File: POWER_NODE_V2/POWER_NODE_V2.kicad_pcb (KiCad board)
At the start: 2 copper layers, 178 x 144 mm, 125 parts, among them J1 CONN_01X02, J10 CONN_02X07, J11 CONN_01X04, J12 CONN_01X04, J13 CONN_01X02, J14 CONN_01X02, J15 CONN_01X02, J16 CONN_01X03, J17 CONN_01X03, J18 CONN_01X03, J19 CONN_01X03, J2 CONN_01X02, J20 CONN_01X03, J21 CONN_01X03, J3 CONN_01X02, J4 CONN_01X02, J5 Booster_J1_J3, J6 I2C2_J10_8_9, J7 Booster_J4_J2, J8 CONN_01X01, J9 CONN_01X02, Q1 BSS84, Q2 BSS84, Q3 BSS84, Q4 BSS84, Q5 BSS84, Q6 BSS84, Q7 BSS84, U1 LM1117MP-3.3/NOPB, U10 DS2482S-100+T&R, U11 DS2482S-100+T&R, U12 NCV8405ADTRKG, U13 MAX14850AEE+, U14 MAX14850AEE+, U15 TL783CKTTR, U16 TL783CKTTR, U17 AMC1100DWV, U18 AMC1100DWV, U19 NUD3124LT1G, U2 R-745.0P, U20 RTE24024, U3 DS2482S-100+T&R, U4 DS2482S-100+T&R, U5 DS2482S-100+T&R, U6 TSYS01, U7 MS5607-02BA03, U8 DS2482S-100+T&R, U9 DS2482S-100+T&R

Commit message: Power Node v2 WIP
TODO: 3d models, double check everything, update connector P/N on
schematics, align boards and drill holes
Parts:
- J1, J13, J14, J15, J2, J9: footprint Pin_Headers:Pin_Header_Straight_1x02_Pitch2.54mm -> rLoop Footprints:TE_1744055-2_3.96_EP_HDR_ASSY_2P_VERT_HT
- J11, J12: footprint Pin_Headers:Pin_Header_Straight_1x04_Pitch2.54mm -> rLoop Footprints:22-04-1041_Molex_4_Pin_Header_2.50mm
- J16, J17, J18, J19, J20, J21: footprint Pin_Headers:Pin_Header_Straight_1x03_Pitch2.54mm -> rLoop Footprints:3-641215-3_3Pin_Latching_Header
- J3, J4: footprint Pin_Headers:Pin_Header_Straight_1x02_Pitch2.54mm -> rLoop Footprints:Keystone_3544-2
- J5: footprint Pin_Headers:Pin_Header_Straight_2x10_Pitch2.54mm -> rLoop Footprints:Booster1_Header_J1_J3
- J6: footprint Pin_Headers:Pin_Header_Straight_1x02_Pitch2.54mm -> Pin_Headers:Pin_Header_Straight_1x02_Pitch2.54mm_SMD_Pin1Left
- J7: footprint Pin_Headers:Pin_Header_Straight_2x10_Pitch2.54mm -> rLoop Footprints:Booster1_J4_J2
- U1: footprint TO_SOT_Packages_SMD:SOT-223-3Lead_TabPin2 -> TO_SOT_Packages_SMD:SOT-223
- U15, U16: footprint TO_SOT_Packages_SMD:TO-263-3_TabPin2 -> TO_SOT_Packages_SMD:TO-263-3_TabPin4
- U2: footprint Socket_Strips:Socket_Strip_Straight_1x12_Pitch2.54mm -> rLoop Footprints:R-745.0P
- moved R13 181.5 mm to (111.2, 35.0)
- moved C21 166.6 mm to (130.0, 147.2), turned to 180 degrees
- moved C23 151.0 mm to (110.2, 157.8)
- moved C24 149.2 mm to (106.5, 157.8)
- moved C22 147.1 mm to (132.5, 138.8), turned to 90 degrees
- moved C27 146.8 mm to (97.8, 57.8), turned to 270 degrees
- moved D6 146.7 mm to (58.2, 29.0), turned to 0 degrees
- moved C26 143.2 mm to (117.8, 157.8)
- moved C20 141.0 mm to (96.0, 157.2), turned to 180 degrees
- moved C25 140.9 mm to (114.0, 157.8)
- moved J13 140.9 mm to (120.5, 29.0), turned to 180 degrees
- moved R20 140.0 mm to (109.5, 155.5), turned to 90 degrees
- moved C14 138.7 mm to (88.0, 150.5)
- moved J9 136.9 mm to (99.0, 29.0), turned to 180 degrees
- moved C19 135.7 mm to (96.2, 147.2), turned to 180 degrees
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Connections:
- C21 pad 1: Net-(C21-Pad1) -> +3V3
- C21 pad 2: Net-(C21-Pad2) -> GND
- C22 pad 1: Net-(C22-Pad1) -> +3V3
- C22 pad 2: Net-(C22-Pad2) -> GND
- C23 pad 1: /Charger Interface/CHG_I_REF -> Net-(C23-Pad1)
- C24 pad 1: /Charger Interface/CHG_I -> Net-(C24-Pad1)
- C25 pad 1: /Charger Interface/BATT_I_REF -> Net-(C25-Pad1)
- C26 pad 1: /Charger Interface/BATT_I -> Net-(C26-Pad1)
- J11 pad 1: Net-(J11-Pad1) -> Net-(C23-Pad1)
- J11 pad 2: Net-(J11-Pad2) -> Net-(C24-Pad1)
- J12 pad 1: Net-(J12-Pad1) -> Net-(C25-Pad1)
- J12 pad 2: Net-(J12-Pad2) -> Net-(C26-Pad1)
- J7 pad 11: /BMS Interface/BMS_ALERT -> /DC Watchdog/DC_WATCHDOG
- J7 pad 17: /DC Watchdog/DC_WATCHDOG -> Net-(J7-Pad17)
- J7 pad 19: Net-(J7-Pad19) -> /BMS Interface/BMS_ALERT
- Q6 pad 3: Net-(Q6-Pad3) -> +3V3
- R17 pad 1: Net-(J11-Pad2) -> Net-(C24-Pad1)
- R18 pad 1: Net-(J12-Pad1) -> Net-(C25-Pad1)
- R19 pad 1: Net-(J12-Pad2) -> Net-(C26-Pad1)
- R20 pad 1: Net-(J11-Pad1) -> Net-(C23-Pad1)
- R21 pad 1: Net-(J11-Pad1) -> /Charger Interface/CHG_I_REF
- R22 pad 1: Net-(J11-Pad2) -> /Charger Interface/CHG_I
- R23 pad 1: Net-(J12-Pad1) -> /Charger Interface/BATT_I_REF
- R24 pad 1: Net-(J12-Pad2) -> /Charger Interface/BATT_I
- R8 pad 2: Net-(R8-Pad2) -> /I2C Devices/I2C2_SCL
- R9 pad 2: Net-(R9-Pad2) -> /I2C Devices/I2C2_SDA
- U10 pad 1: Net-(U10-Pad1) -> +3V3
- U10 pad 4: Net-(R8-Pad2) -> /I2C Devices/I2C2_SCL
- U10 pad 5: Net-(R9-Pad2) -> /I2C Devices/I2C2_SDA
- U11 pad 4: Net-(R8-Pad2) -> /I2C Devices/I2C2_SCL
- U11 pad 5: Net-(R9-Pad2) -> /I2C Devices/I2C2_SDA
- U18 pad 2: Net-(R15-Pad1) -> CHARGE_N_HOT
- U3 pad 4: /I2C Devices/I2C1_SCL -> /I2C Devices/I2C1_SDA
- U3 pad 5: /I2C Devices/I2C1_SDA -> /I2C Devices/I2C1_SCL
- U4 pad 1: Net-(U4-Pad1) -> +3V3
- U7 pad 7: /I2C Devices/I2C1_SDA -> /I2C Devices/I2C1_SCL
- U7 pad 8: /I2C Devices/I2C1_SCL -> /I2C Devices/I2C1_SDA
- U8 pad 4: Net-(R8-Pad2) -> /I2C Devices/I2C2_SCL
- U8 pad 5: Net-(R9-Pad2) -> /I2C Devices/I2C2_SDA
- U9 pad 4: Net-(R8-Pad2) -> /I2C Devices/I2C2_SCL
- U9 pad 5: Net-(R9-Pad2) -> /I2C Devices/I2C2_SDA
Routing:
- net +3V3: track 0.00 -> 509.9 mm, vias 0 -> 13
- net +24V: track 0.00 -> 199.7 mm
- net +5V: track 0.00 -> 130.8 mm
- net Net-(C26-Pad1): track 0.00 -> 117.0 mm
- net /RM57 Core/CHG_RLY: track 0.00 -> 112.9 mm
- net Net-(C23-Pad1): track 0.00 -> 112.2 mm
- net Net-(C24-Pad1): track 0.00 -> 111.9 mm
- net Net-(C25-Pad1): track 0.00 -> 111.6 mm
- net /1-Wire Connectors/ONE_WIRE_BATT_10_12: track 0.00 -> 110.4 mm
- net /BMS Interface/BMS_MISO: track 0.00 -> 108.9 mm, vias 0 -> 2
- net /BMS Interface/BMS_MOSI: track 0.00 -> 107.9 mm, vias 0 -> 2
- net /1-Wire Connectors/ONE_WIRE_BATT_7_9: track 0.00 -> 104.1 mm
- net /BMS Interface/BMS_NCS: track 0.00 -> 100.0 mm, vias 0 -> 2
- net /BMS Interface/BMS_DRDY: track 0.00 -> 94.4 mm, vias 0 -> 2
- net /1-Wire Connectors/ONE_WIRE_BATT_13_15: track 0.00 -> 93.5 mm
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- added copper zone on F.Cu, net +24V
- added copper zone on B.Cu, net GND
- added copper zone on F.Cu, net GND
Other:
- net class 24V_High_Current added: clearance 0.2, trace_width 10, via_dia 12, via_drill 10
- net class Default: via_dia 0.6 -> 0.6858; via_drill 0.4 -> 0.3302
- rule trace_min: 0.2 -> 0.1524
- rule via_min_drill: 0.3 -> 0.3302
- rule via_min_size: 0.4 -> 0.6858

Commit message: 3d WIP
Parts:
- U20: footprint rLoop Footprints:RTE24024 -> rLoop_Footprints:RTE24024
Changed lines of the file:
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@@
   )
   (setup
-    (last_trace_width 2)
+    (last_trace_width 0.25)
     (user_trace_width 2)
     (user_trace_width 4)
@@
     )
   )
-  (module "rLoop Footprints:RTE24024" (layer F.Cu)
-    (at 45.25 80.75 90)
-    (fp_text reference U20 (at 0 8.8 90) (layer F.SilkS)
-      (effects (font (size 1 1) (thickness 0.15)))
-    )
-    (fp_text value RTE24024 (at 0 -8.8 90) (layer F.Fab)
-      (effects (font (size 1 1) (thickness 0.15)))
-    )
-    (fp_line (start -7.56 -7.5) (end 22.68 -7.5) (layer F.SilkS) (width 0.1))
-    (fp_line (start 22.68 -7.5) (end 22.68 7.5) (layer F.SilkS) (width 0.1))
-    (fp_line (start 22.68 7.5) (end -7.56 7.5) (layer F.SilkS) (width 0.1))
-    (fp_line (start -7.56 7.5) (end -7.56 -7.5) (layer F.SilkS) (width 0.1))
-    (pad A2 thru_hole circle (at -5.18 3.75 90) (size 2 2) (drill 1.3) (layers *.Cu *.Mask)
-      (net 19 "Net-(D7-Pad2)"))
-    (pad A1 thru_hole circle (at -5.18 -3.75 90) (size 2 2) (drill 1.3) (layers *.Cu *.Mask)
-      (net 3 +24V))
-    (pad 11 thru_hole circle (at 15.12 -3.75 90) (size 2 2) (drill 1.3) (layers *.Cu *.Mask)
-      (net 3 +24V))
-    (pad 14 thru_hole circle (at 20.16 -3.75 90) (size 2 2) (drill 1.3) (layers *.Cu *.Mask)
-      (net 20 "Net-(D8-Pad2)"))
-    (pad 24 thru_hole circle (at 20.16 3.75 90) (size 2 2) (drill 1.3) (layers *.Cu *.Mask)
-      (net 103 "Net-(U20-Pad24)"))
-    (pad 21 thru_hole circle (at 15.12 3.75 90) (size 2 2) (drill 1.3) (layers *.Cu *.Mask)
-      (net 104 "Net-(U20-Pad21)"))
-    (pad 22 thru_hole circle (at 10.08 3.75 90) (size 2 2) (drill 1.3) (layers *.Cu *.Mask)
-      (net 105 "Net-(U20-Pad22)"))
-    (pad 12 thru_hole circle (at 10.08 -3.75 90) (size 2 2) (drill 1.3) (layers *.Cu *.Mask)
-      (net 106 "Net-(U20-Pad12)"))
-  )
   (module "rLoop Footprints:2920L300_15DR" (layer F.Cu)
     (at 69.75 154.75)
@@
       (at (xyz 0 0 0))
       (scale (xyz 1 1 1))
-      (rotate (xyz 0 0 0))
+      (rotate (xyz 0 0 90))
     )
   )
@@
       (at (xyz 0 0 0))
       (scale (xyz 1 1 1))
-      (rotate (xyz 0 0 0))
+      (rotate (xyz 0 0 90))
     )
   )
@@
       (at (xyz 0 0 0))
       (scale (xyz 1 1 1))
-      (rotate (xyz 0 0 0))
+      (rotate (xyz 0 0 90))
     )
   )
@@
       (at (xyz 0 0 0))
       (scale (xyz 1 1 1))
-      (rotate (xyz 0 0 0))
+      (rotate (xyz 0 0 90))
     )
   )
@@
       (at (xyz 0 0 0))
       (scale (xyz 1 1 1))
-      (rotate (xyz 0 0 0))
+      (rotate (xyz 0 0 90))
     )
   )
@@
       (at (xyz 0 0 0))
       (scale (xyz 1 1 1))
-      (rotate (xyz 0 0 0))
+      (rotate (xyz 0 0 90))
     )
   )
@@
     (model ${KISYS3DMOD}/TO_SOT_Packages_SMD.3dshapes/SOT-223.wrl
       (at (xyz 0 0 0))
-      (scale (xyz 1 1 1))
-      (rotate (xyz 0 0 0))
+      (scale (xyz 0.393701 0.393701 0.393701))
+      (rotate (xyz 0 0 90))
     )
   )
@@
       (at (xyz 0 0 0))
       (scale (xyz 1 1 1))
-      (rotate (xyz 0 0 0))
+      (rotate (xyz 0 0 90))
     )
   )
@@
     (model ${KISYS3DMOD}/TO_SOT_Packages_SMD.3dshapes/SOT-223.wrl
       (at (xyz 0 0 0))
-      (scale (xyz 1 1 1))
-      (rotate (xyz 0 0 0))
+      (scale (xyz 0.393701 0.393701 0.393701))
+      (rotate (xyz 0 0 90))
     )
   )
@@
       (net 16 "Net-(D4-Pad2)"))
   )
+  (module rLoop_Footprints:RTE24024 (layer F.Cu)
+    (at 45.25 80.75 90)
+    (fp_text reference U20 (at -6.6 7.5 90) (layer F.SilkS)
+      (effects (font (size 1 1) (thickness 0.15)))
+    )
+    (fp_text value RTE24024 (at -4 -7.6 90) (layer F.Fab)
+      (effects (font (size 1 1) (thickness 0.15)))
+    )
+    (fp_line (start 22.2 -6.4) (end -7.8 -6.4) (layer F.SilkS) (width 0.15))
+    (fp_line (start -7.8 6.4) (end 22.2 6.4) (layer F.SilkS) (width 0.15))
+    (fp_line (start 22.2 -6.4) (end 22.2 6.4) (layer F.SilkS) (width 0.15))
+    (fp_line (start -7.8 -6.4) (end -7.8 6.4) (layer F.SilkS) (width 0.15))
+    (pad A2 thru_hole circle (at -5.18 3.75 90) (size 2 2) (drill 1.3) (layers *.Cu *.Mask)
+      (net 19 "Net-(D7-Pad2)"))
+    (pad A1 thru_hole circle (at -5.18 -3.75 90) (size 2 2) (drill 1.3) (layers *.Cu *.Mask)
+      (net 3 +24V))
+    (pad 11 thru_hole circle (at 15.12 -3.75 90) (size 2 2) (drill 1.3) (layers *.Cu *.Mask)
+      (net 3 +24V))
+    (pad 14 thru_hole circle (at 20.16 -3.75 90) (size 2 2) (drill 1.3) (layers *.Cu *.Mask)
+      (net 20 "Net-(D8-Pad2)"))
+    (pad 24 thru_hole circle (at 20.16 3.75 90) (size 2 2) (drill 1.3) (layers *.Cu *.Mask)
+      (net 103 "Net-(U20-Pad24)"))
+    (pad 21 thru_hole circle (at 15.12 3.75 90) (size 2 2) (drill 1.3) (layers *.Cu *.Mask)
+      (net 104 "Net-(U20-Pad21)"))
+    (pad 22 thru_hole circle (at 10.08 3.75 90) (size 2 2) (drill 1.3) (layers *.Cu *.Mask)
+      (net 105 "Net-(U20-Pad22)"))
+    (pad 12 thru_hole circle (at 10.08 -3.75 90) (size 2 2) (drill 1.3) (layers *.Cu *.Mask)
+      (net 106 "Net-(U20-Pad12)"))
+    (model ${KIPRJMOD}/3d-models/RTE24024.wrl
+      (at (xyz 0 0 0))
+      (scale (xyz 1 1 1))
+      (rotate (xyz 0 0 0))
+    )
+  )
   (gr_line (start 29 168) (end 29 24) (angle 90) (layer Edge.Cuts) (width 0.15))

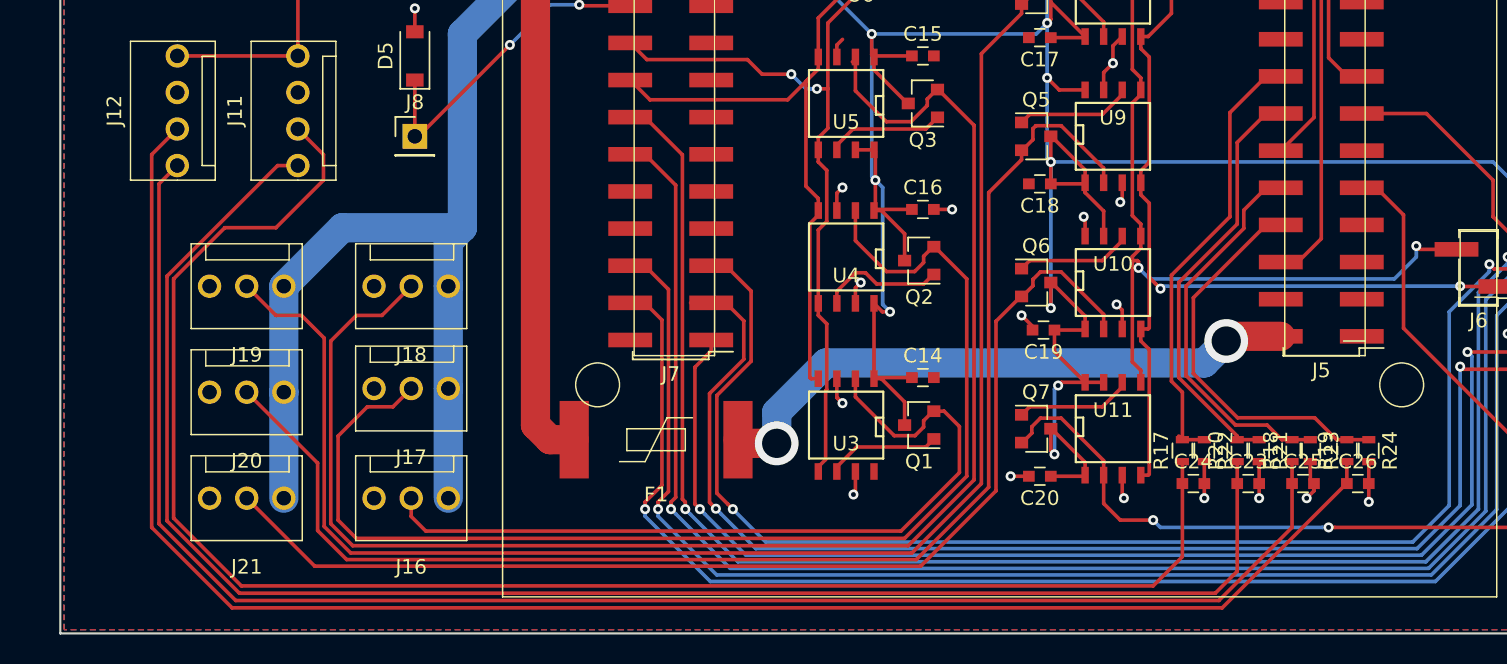
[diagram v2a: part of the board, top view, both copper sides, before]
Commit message: 3d model work
TODO: change 2 pins to MTA156
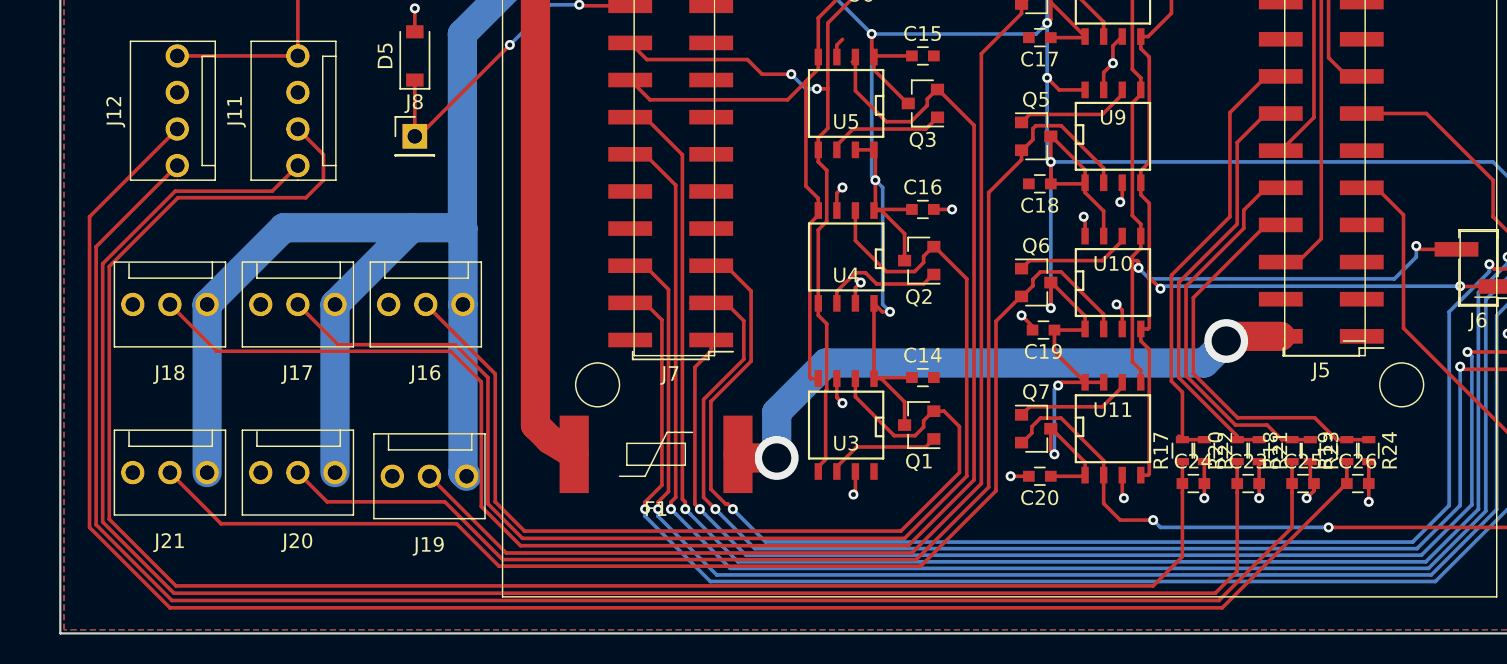
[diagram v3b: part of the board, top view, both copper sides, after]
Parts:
- J11, J12: footprint rLoop Footprints:22-04-1041_Molex_4_Pin_Header_2.50mm -> rLoop_Footprints:22-04-1041_Molex_4_Pin_Header_2.50mm
- J16, J17, J18, J19, J20, J21: footprint rLoop Footprints:3-641215-3_3Pin_Latching_Header -> rLoop_Footprints:3-641215-3_3Pin_Latching_Header
- J3, J4: footprint rLoop Footprints:Keystone_3544-2 -> rLoop_Footprints:Keystone_3544-2
- U2: footprint rLoop Footprints:R-745.0P -> rLoop_Footprints:R-745.0P
- moved J19 18.0 mm to (54.2, 157.2)
- moved J18 16.5 mm to (36.5, 145.5)
- moved J16 13.3 mm to (54.0, 145.5)
- moved J17 9.65 mm to (45.2, 145.5)
- moved J20 6.52 mm to (45.2, 157.0)
- moved J21 5.53 mm to (36.5, 157.0)
- moved F1 1.00 mm to (69.8, 155.8)
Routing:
- net /1-Wire Connectors/ONE_WIRE_BATT_10_12: track 110.4 -> 84.9 mm
- net +3V3: track 509.9 -> 529.8 mm
- net Net-(C24-Pad1): track 111.9 -> 121.2 mm
- net Net-(C23-Pad1): track 112.2 -> 121.5 mm
- net /1-Wire Connectors/ONE_WIRE_BATT_1_3: track 55.1 -> 64.0 mm
- net /1-Wire Connectors/ONE_WIRE_BATT_13_15: track 93.5 -> 85.0 mm
- net Net-(C25-Pad1): track 111.6 -> 117.7 mm
- net Net-(C26-Pad1): track 117.0 -> 123.0 mm
- net /1-Wire Connectors/ONE_WIRE_BATT_16_18: track 78.4 -> 84.4 mm
- net /1-Wire Connectors/ONE_WIRE_BATT_7_9: track 104.1 -> 106.7 mm
- net /1-Wire Connectors/ONE_WIRE_BATT_4_6: track 83.6 -> 85.4 mm
- net Net-(F1-Pad2): track 41.5 -> 42.5 mm

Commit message: Lot's of progress
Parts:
- removed C11: 330uF / 35V / 20% / SMD 10x10, Capacitors_SMD:C_0603
- added Power_Node_Mounting_Holes: Power_Node_Mounting_Holes, rLoop_Footprints:Power_Node_Mounting_Holes, F.Cu at (33.2, 163.7)
- added RM57_Mounting_Holes: RM57_Mounting_Holes, rLoop_Footprints:RM57_Mounting_Hole, F.Cu at (66.6, 151.8)
- D1, D10, D11, D12, D2, D8: footprint rLoop Footprints:LED_0805 -> rLoop_Footprints:LED_0805
- D3, D4: value AS4PM-M3/86A -> FES10G; footprint rLoop Footprints:TO-277A_SMPC -> rLoop_Footprints:TO-277A_SMPC
- J1, J13, J14, J15, J2, J9: value CONN_01X02 -> TE_3-641119-2; footprint rLoop Footprints:TE_1744055-2_3.96_EP_HDR_ASSY_2P_VERT_HT -> rLoop_Footprints:3-641119-2_TE_2P_MTA156_HDR
- J16, J17, J18, J19, J20, J21: value CONN_01X03 -> 3-641215-3
- J3, J4: value CONN_01X02 -> Keystone_3544-2
- J5: value Booster_J1_J3 -> 5-146130-9; footprint rLoop Footprints:Booster1_Header_J1_J3 -> rLoop_Footprints:Booster1_Header_J1_J3
- J7: value Booster_J4_J2 -> 5-146130-9; footprint rLoop Footprints:Booster1_J4_J2 -> rLoop_Footprints:Booster1_J4_J2
- RM_57_Outline: renamed from REF**; footprint rLoop Footprints:RM57_Launchpad_Outline -> rLoop_Footprints:RM57_Launchpad_Outline
- U17, U18: footprint rLoop Footprints:amc1100_SOIC8 -> rLoop_Footprints:amc1100_SOIC8
- U6: footprint rLoop Footprints:QFN16_4x4 -> rLoop_Footprints:QFN16_4x4
- U7: footprint rLoop Footprints:ms5607-02ba03 -> rLoop_Footprints:ms5607-02ba03
- moved RM_57_Outline 72.8 mm to (127.0, 35.0)
- moved F1 16.2 mm to (62.0, 141.5), turned to 270 degrees
- moved U12 6.50 mm to (65.0, 63.5)
- moved R10 6.25 mm to (62.5, 70.0)
- moved R5 5.50 mm to (37.2, 85.5), turned to 90 degrees
- moved R3 4.87 mm to (37.0, 82.0)
- moved J9 4.24 mm to (103.2, 28.4)
- moved J1 3.96 mm to (41.0, 27.7)
- moved J14 2.86 mm to (112.8, 28.4)
- moved C4 2.48 mm to (61.0, 107.2)
- moved D12 2.28 mm to (33.0, 85.0)
- moved C1 2.00 mm to (37.2, 113.7), turned to 180 degrees
- moved J13 1.80 mm to (122.2, 28.4)
- moved R16 1.73 mm to (121.2, 39.2)
- moved R15 1.70 mm to (122.2, 35.8)
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- renumbered REF** to BMS_Outline
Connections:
- J13 pad 1: CHARGE_P_HOT -> CHARGE_N_HOT
- J13 pad 2: CHARGE_N_HOT -> CHARGE_P_HOT
- J14 pad 1: BATT_P_HOT -> BATT_N_HOT
- J14 pad 2: BATT_N_HOT -> BATT_P_HOT
- J15 pad 1: Net-(D8-Pad2) -> GND
- J15 pad 2: GND -> Net-(D8-Pad2)
- J9 pad 1: +24V -> Net-(D6-Pad2)
- J9 pad 2: Net-(D6-Pad2) -> +24V
- U17 pad 2: Net-(R13-Pad2) -> BATT_N_HOT
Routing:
- net BATT_N_HOT: track 65.3 -> 115.8 mm
- net Net-(R13-Pad2): track 56.3 -> 9.29 mm
- net +5V: track 131.1 -> 109.2 mm
- net Net-(F1-Pad2): track 42.5 -> 61.4 mm
- net +24V: track 199.7 -> 187.5 mm
- net Net-(D6-Pad2): track 53.6 -> 63.4 mm
- net Net-(J1-Pad2): track 10.3 -> 16.1 mm
- net /BMS Interface/BMS_FAN: track 65.1 -> 59.4 mm
- net GND: track 66.5 -> 72.2 mm, vias 37 -> 39
- net +3V3: track 529.8 -> 534.8 mm
- net Net-(C24-Pad1): track 121.2 -> 117.8 mm
- net Net-(C23-Pad1): track 121.5 -> 118.2 mm
- net CHARGE_P_HOT: track 29.3 -> 32.4 mm
- net Net-(C25-Pad1): track 117.7 -> 114.7 mm
- net Net-(C26-Pad1): track 123.0 -> 120.1 mm
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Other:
- board text added: "Remove JP6 from Launchpad for using node power."
- board text added: "Use No. 2 or M2 screws for mounting RM57."
